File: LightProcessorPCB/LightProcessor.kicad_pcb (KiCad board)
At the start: 4 copper layers, 192.1 x 182.1 mm, 131 parts, among them IC1 STM32G474RET6, J1 USB_C_Receptacle_USB2.0_16P, J2 PJ-202B, SW10 Tactile_6mm, SW11 SW_SP5T_NR01105, SW7 SW_SP5T_NR01105, SW8 SW_SP5T_NR01105, SW9 SW_SP5T_NR01105, U1 STLINK-V3MODS, U10 SN74HC4066N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

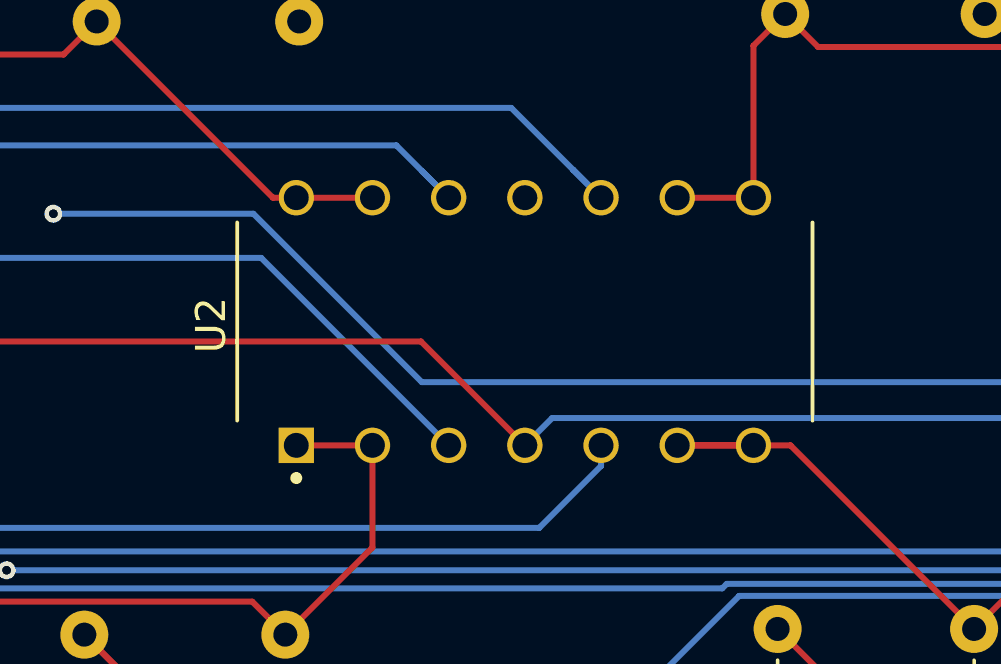
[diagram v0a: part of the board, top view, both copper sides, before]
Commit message: Relocate Stack Pointer
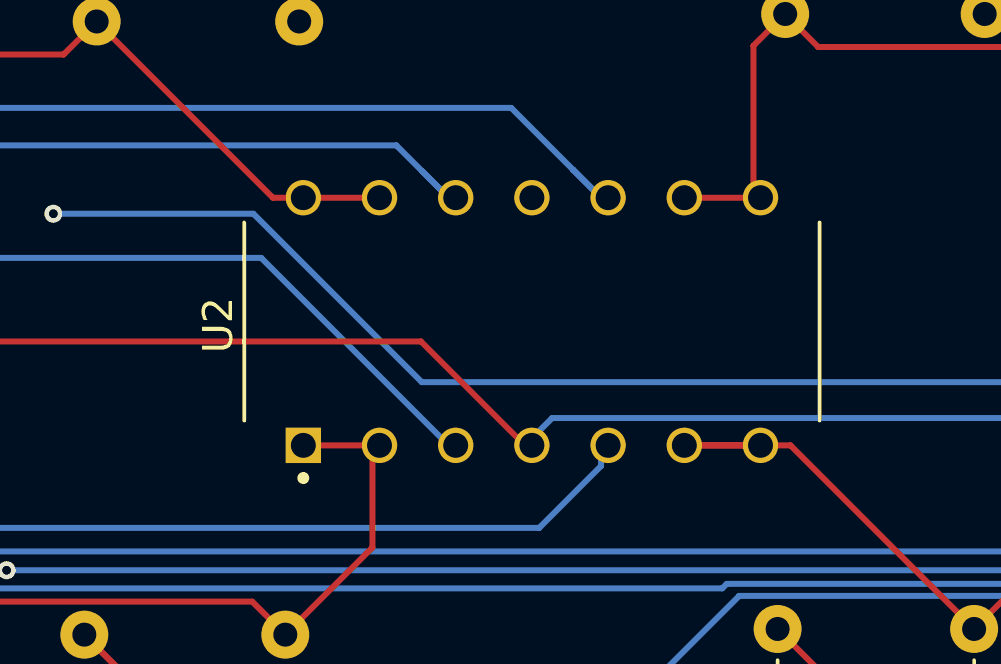
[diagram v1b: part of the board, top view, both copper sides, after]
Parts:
- moved U2 0.24 mm to (180.7, 155.1)
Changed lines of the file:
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@@
 	(footprint "LM324N_NOPB:DIP825W47P254L1917H533Q14"
 		(layer "F.Cu")
-		(at 180.5 155.0883 90)
+		(at 180.735 155.0883 90)
 		(property "Reference" "U2"
 			(at -0.1225 -10.46025 90)
